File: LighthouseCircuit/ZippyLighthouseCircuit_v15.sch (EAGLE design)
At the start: 23 parts

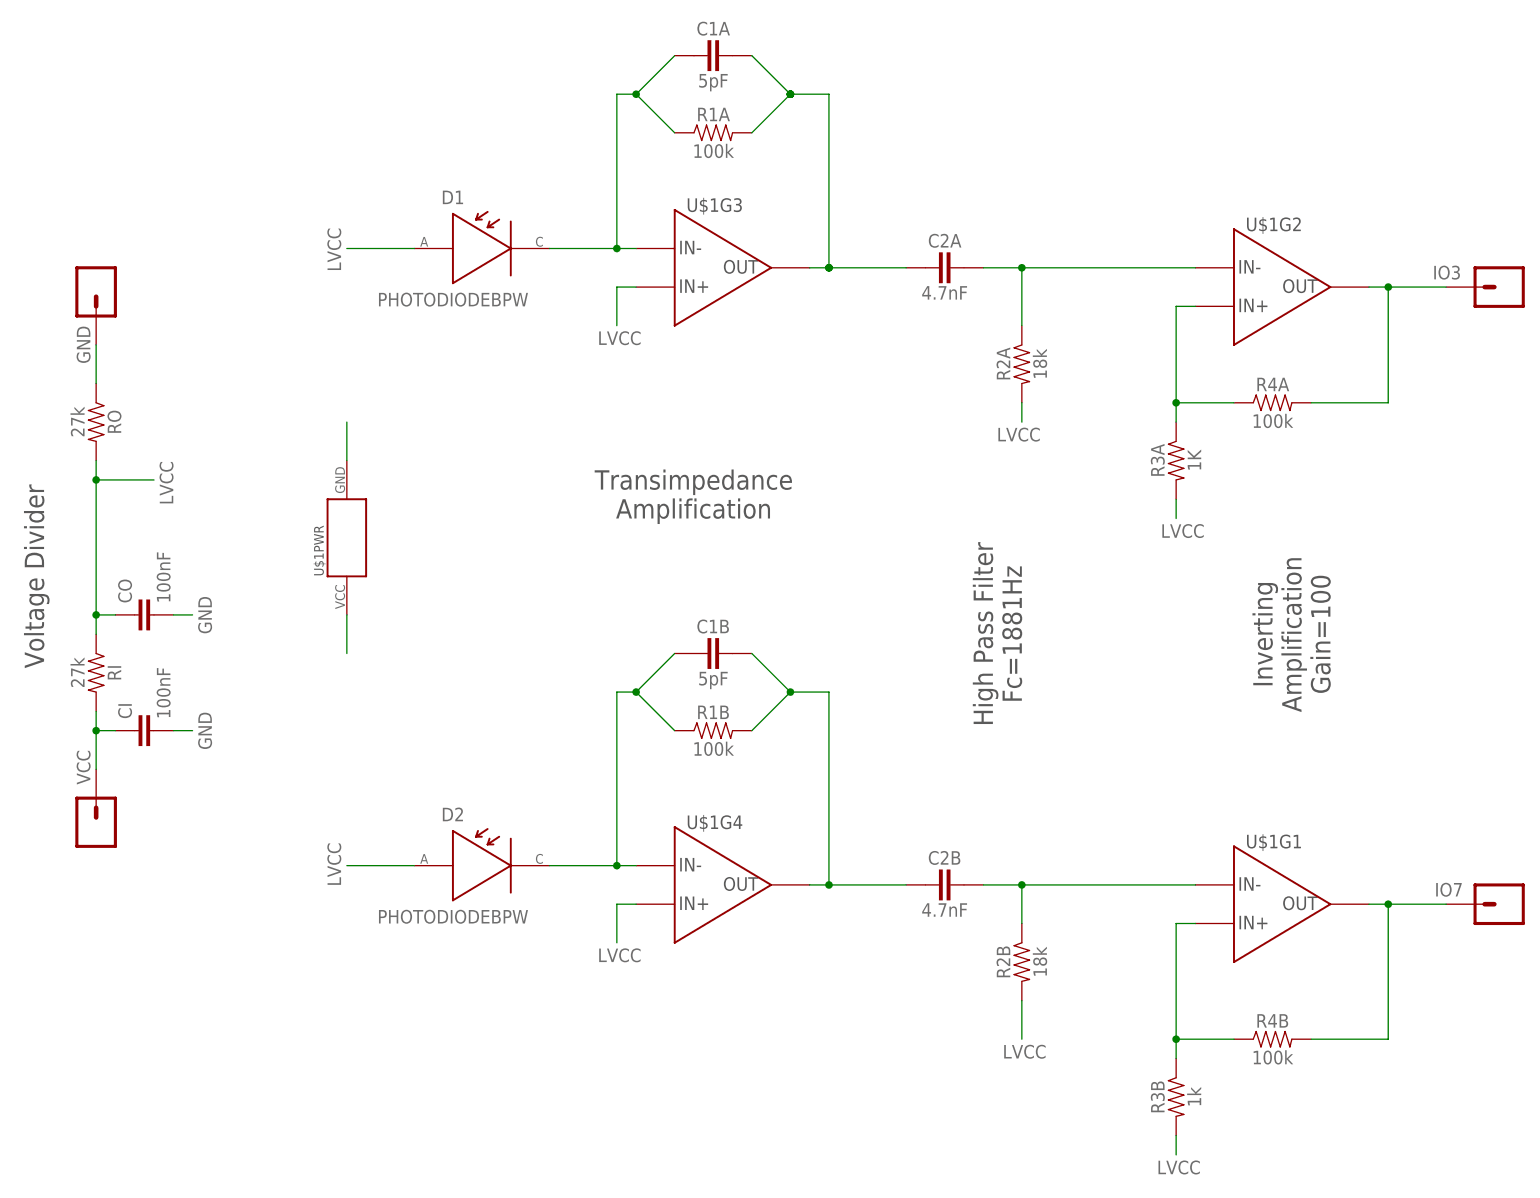
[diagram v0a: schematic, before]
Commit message: Significant changes and refactored codebase layout. Improvements made to path following, PID control, path execution, added a new default path, and many other changes.
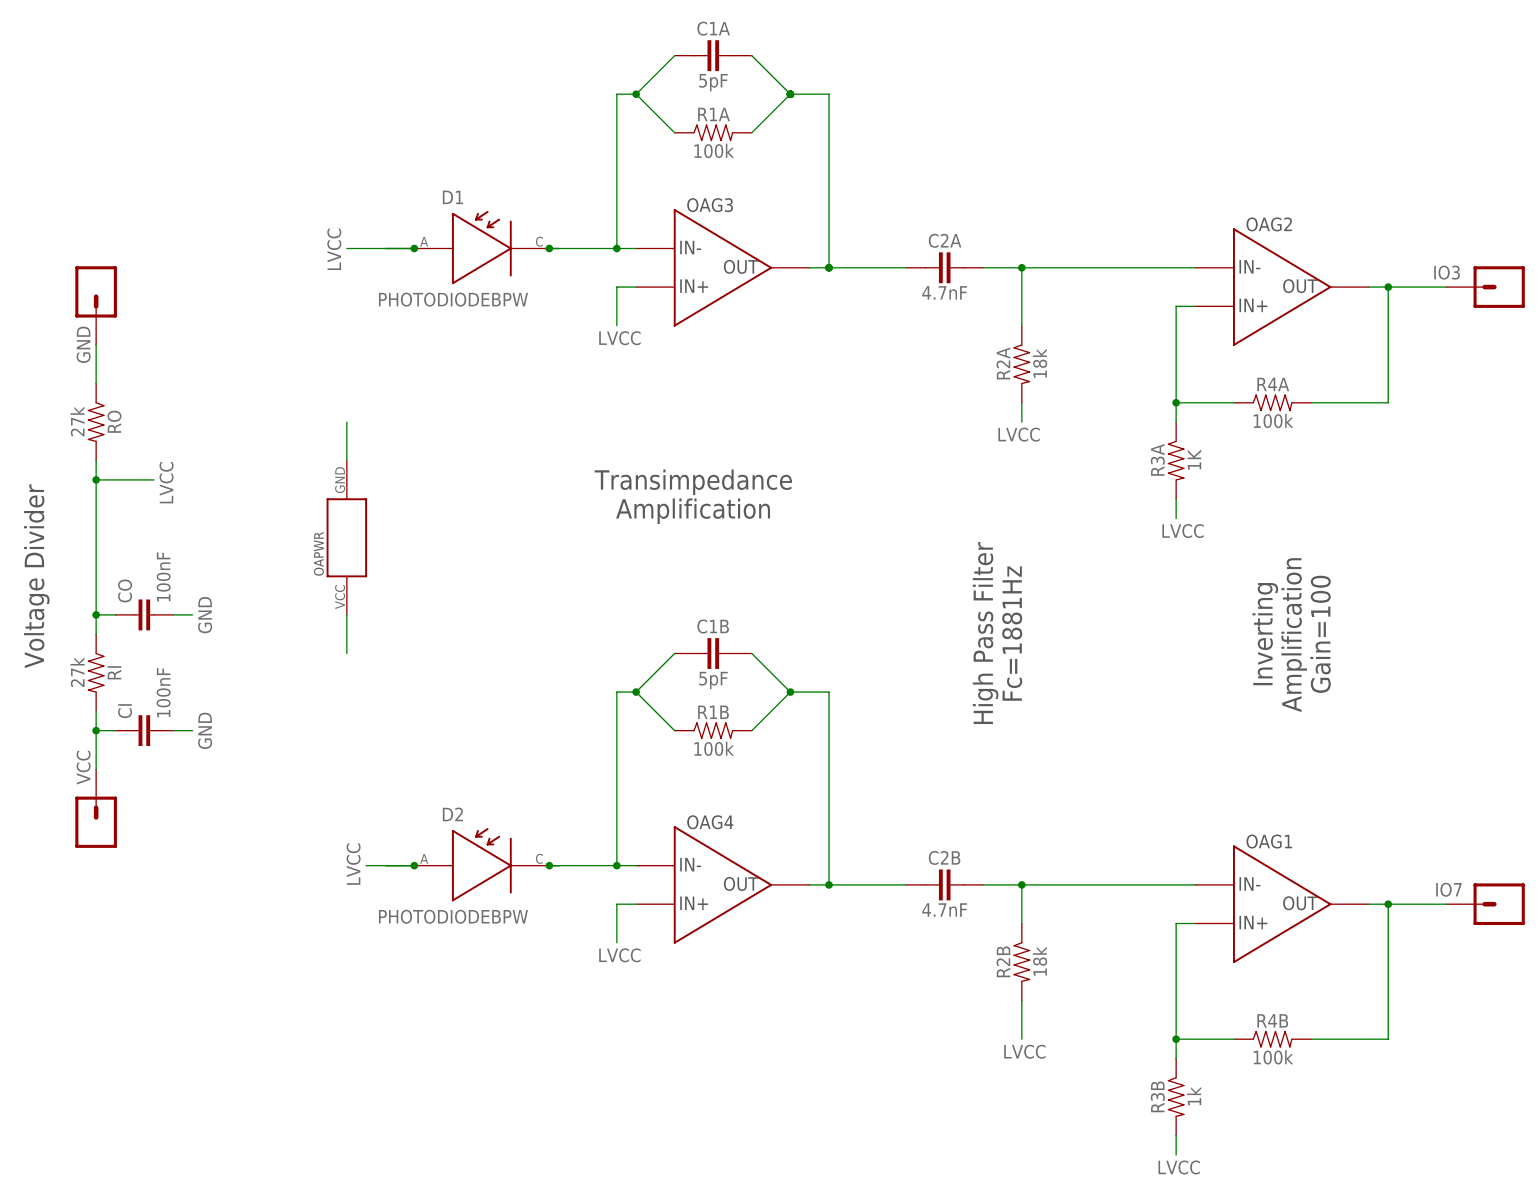
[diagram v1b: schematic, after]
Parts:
- removed U$1: TLV2464IPW, ZippyComponentLibrary:TLV2464IPW
- added OA: TLV2464IDM, ZippyComponentLibrary:TLV2464IDM
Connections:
- net D1IN: now also OAG4.IN-; no longer U$1G4.IN-
- net D1OA2P: now also OAG1.IN-; no longer U$1G1.IN-
- net D1OAOUT1: now also OAG4.OUT; no longer U$1G4.OUT
- net D2IN: now also OAG3.IN-; no longer U$1G3.IN-
- net D2OA1OUT: now also OAG3.OUT; no longer U$1G3.OUT
- net D2OA2N: now also OAG2.IN+; no longer U$1G2.IN+
- net D2OA2P: now also OAG2.IN-; no longer U$1G2.IN-
- net GND: now also OAPWR.GND; no longer U$1PWR.GND
- net IO3: now also OAG2.OUT; no longer U$1G2.OUT
- net IO7: now also OAG1.OUT; no longer U$1G1.OUT
- net LVCC: now also OAG3.IN+, OAG4.IN+; no longer U$1G3.IN+, U$1G4.IN+
- net N$11: now also OAG1.IN+; no longer U$1G1.IN+
- net VCC: now also OAPWR.VCC; no longer U$1PWR.VCC
